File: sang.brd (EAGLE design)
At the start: 100 x 80 mm, 39 parts, among them IC1 L293D, IC2 L293D, IC3 NE555, IC4 L293D, Q1 16MHz

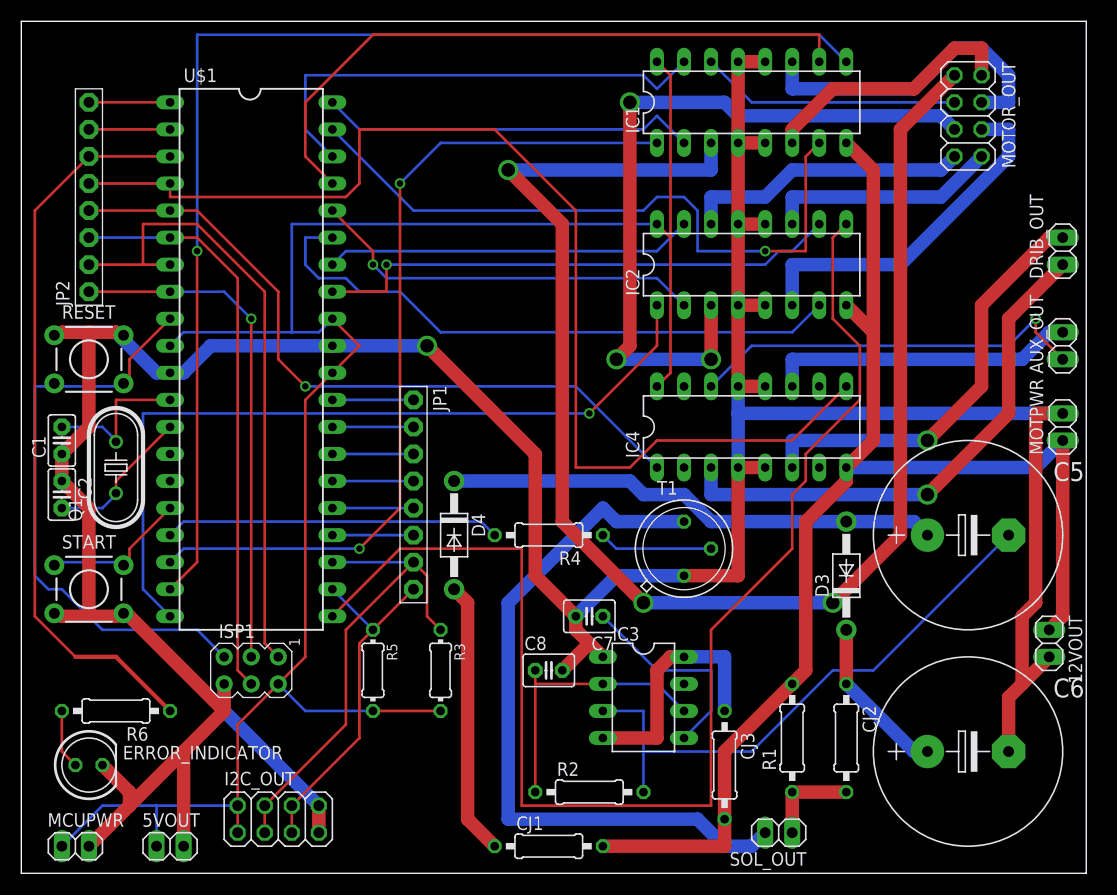
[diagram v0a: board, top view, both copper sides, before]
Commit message: Alpha 1
Branding and layout changed
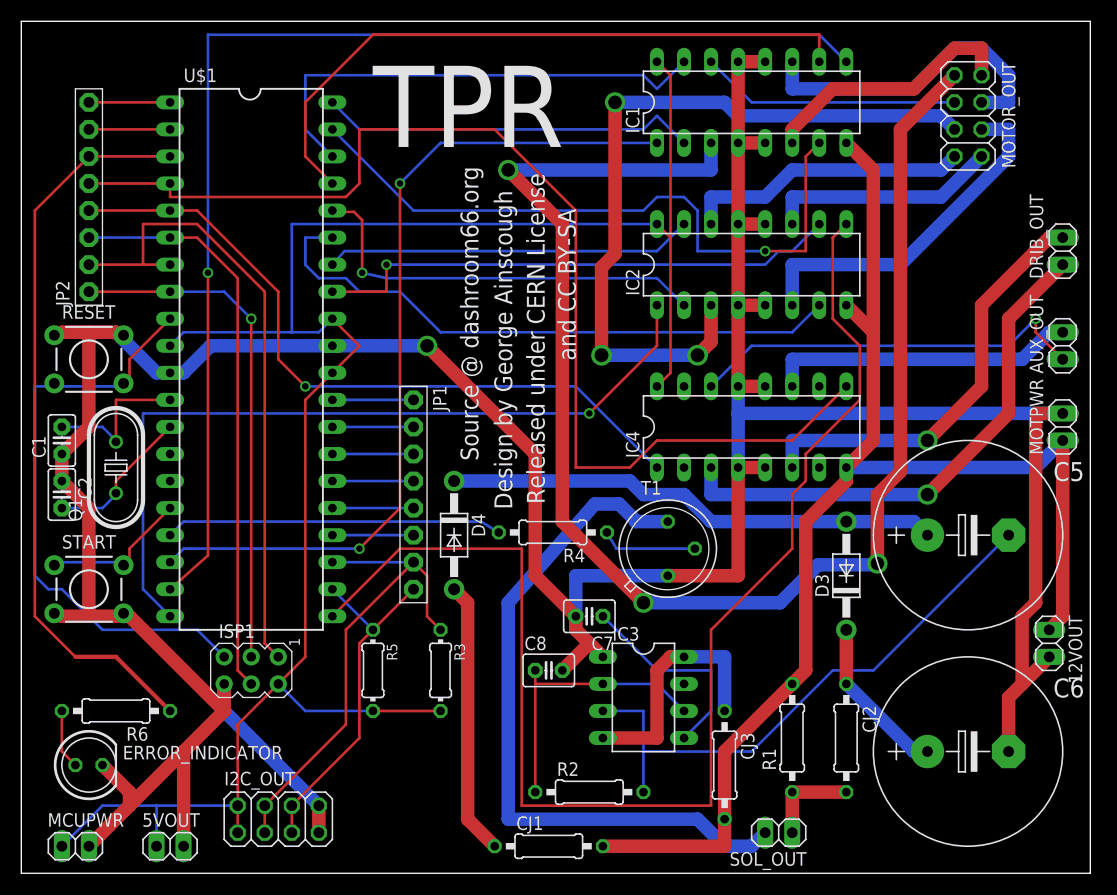
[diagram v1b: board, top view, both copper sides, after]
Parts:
- moved T1 1.52 mm to (60.7, 30.5)
- moved R4 0.46 mm to (49.9, 32.0)
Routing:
- net GND: track 329.1 -> 331.3 mm
- net M3F: track 37.4 -> 39.4 mm
- net N$4: track 10.7 -> 9.13 mm
- net M3+: track 70.2 -> 71.4 mm
- net N$7: track 66.7 -> 66.0 mm
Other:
- board size 100 x 80 mm -> 100.4 x 80 mm
- board text added: "Design by George Ainscough"
- board text added: "Released under CERN License"
- board text added: "Source @ dashroom66.org"
- board text added: "TPR"
- board text added: "and CC BY-SA"
